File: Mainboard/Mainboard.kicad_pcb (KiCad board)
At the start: 4 copper layers, 78.8 x 40 mm, 55 parts, among them IC1 IP5306, J1 2479774-2, J3 Conn_01x06_Pin, U1 LM3880, U2 MAX98357A, U3 TPS22917DBV, U4 TLV62569DBV, U5 W25Q128JVS, U6 TLV75518PDBV, U7 TPS62822DLC

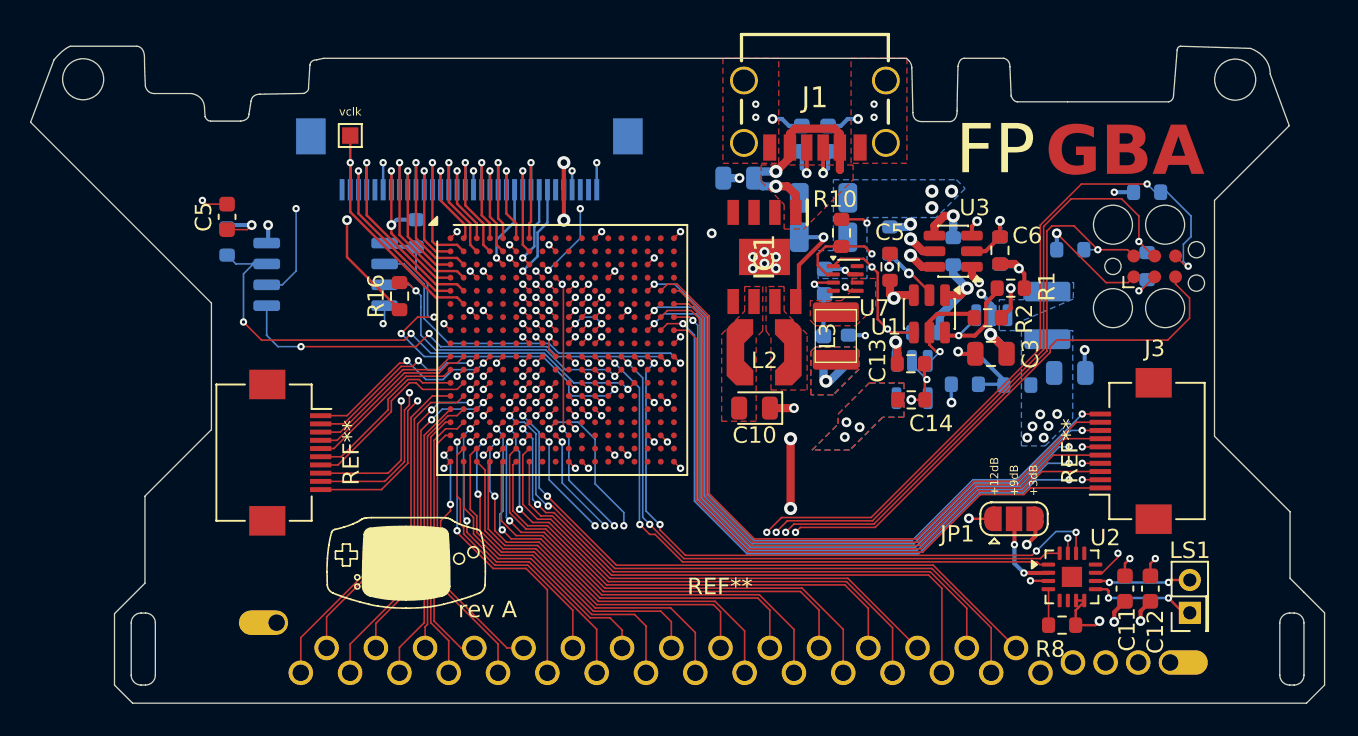
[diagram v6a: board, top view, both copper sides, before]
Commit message: + Power sw, + R arrays, sync PCB/schem
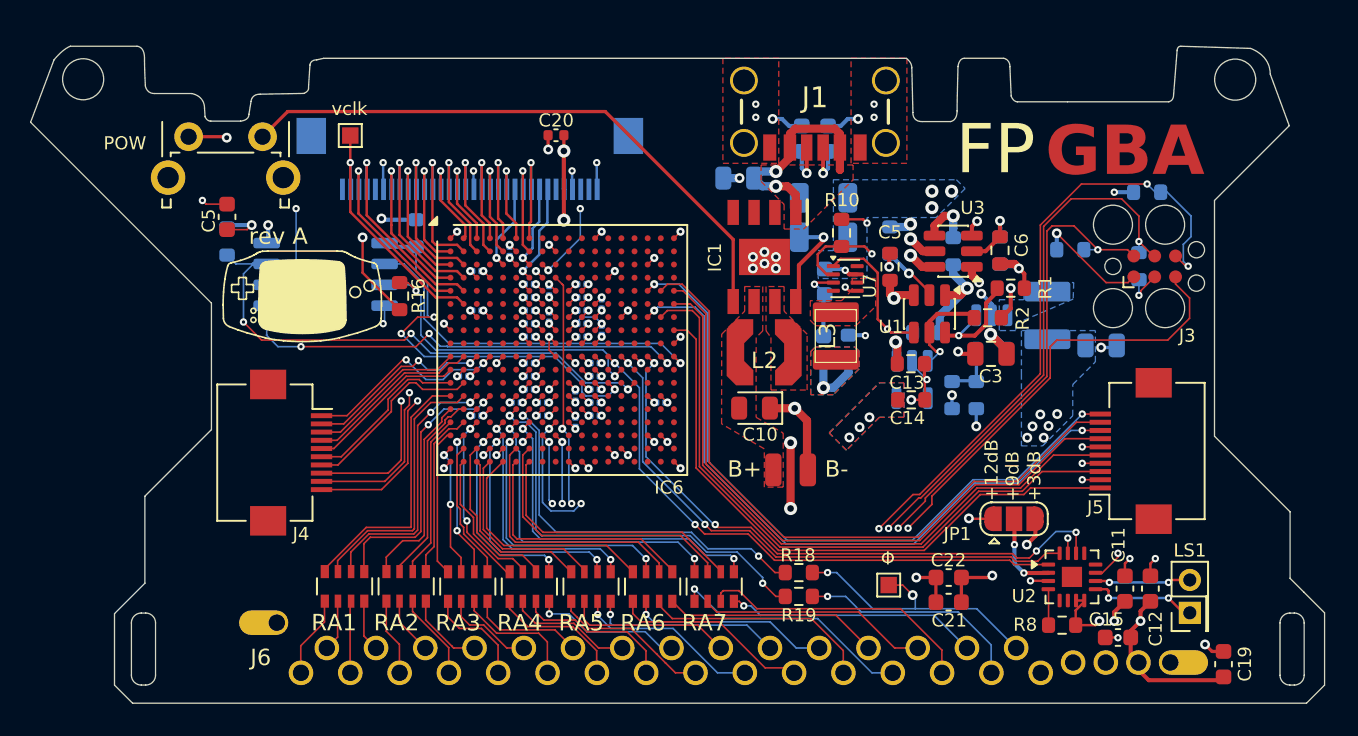
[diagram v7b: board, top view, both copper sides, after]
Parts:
- removed the REF** at (118.4, 77.1)
- removed the REF** at (153.0, 83.2)
- removed the REF** at (128.0, 92.0)
- removed the REF** at (101.8, 83.3)
- removed the REF** at (112.8, 65.5)
- added B+: SolderWirePad_1x01_SMD_1x2mm, Connector_Wire:SolderWirePad_1x01_SMD_1x2mm, F.Cu at (131.2, 84.4)
- added B-: SolderWirePad_1x01_SMD_1x2mm, Connector_Wire:SolderWirePad_1x01_SMD_1x2mm, F.Cu at (133.3, 84.4)
- added C15: 100nF, Capacitor_SMD:C_0603_1608Metric, F.Cu at (152.2, 94.6)
- added C19: 100nF, Capacitor_SMD:C_0603_1608Metric, F.Cu at (158.7, 96.2)
- added C20: 100nF, Capacitor_SMD:C_0402_1005Metric, F.Cu at (118.0, 64.0)
- added C21: 100nF, Capacitor_SMD:C_0603_1608Metric, F.Cu at (141.9, 92.5)
- added C22: 10uF, Capacitor_SMD:C_0603_1608Metric, F.Cu at (141.9, 91.0)
- added IC6: XC7S50-L1CSGA324I, Package_BGA:BGA-324_15x15mm_Layout18x18_P0.8mm, F.Cu at (118.4, 77.1)
- added J4: Left Daughter Connector, Connector_FFC-FPC:Hirose_FH12-10S-0.5SH_1x10-1MP_P0.50mm_Horizontal, F.Cu at (101.9, 83.3)
- added J5: Right Daughter Connector, Connector_FFC-FPC:Hirose_FH12-10S-0.5SH_1x10-1MP_P0.50mm_Horizontal, F.Cu at (153.0, 83.2)
- added J6: CART, AGBRE:AGB Cart Pin, F.Cu at (128.0, 92.0)
- added J9: Screen zif FFC/FPC, Connector_FFC-FPC:Hirose_FH12-32S-0.5SH_1x32-1MP_P0.50mm_Horizontal, B.Cu at (112.8, 65.5)
- added R18: 22, Resistor_SMD:R_0603_1608Metric, F.Cu at (132.8, 90.7)
- added R19: 22, Resistor_SMD:R_0603_1608Metric, F.Cu at (132.8, 92.1)
- added RA1: 22, Resistor_SMD:R_Array_Convex_4x0603, F.Cu at (105.2, 91.5)
- added RA2: 22, Resistor_SMD:R_Array_Convex_4x0603, F.Cu at (108.9, 91.5)
- added RA3: 22, Resistor_SMD:R_Array_Convex_4x0603, F.Cu at (112.7, 91.5)
- added RA4: 22, Resistor_SMD:R_Array_Convex_4x0603, F.Cu at (116.4, 91.5)
- added RA5: 22, Resistor_SMD:R_Array_Convex_4x0603, F.Cu at (120.2, 91.5)
- added RA6: 22, Resistor_SMD:R_Array_Convex_4x0603, F.Cu at (123.9, 91.5)
- added RA7: 22, Resistor_SMD:R_Array_Convex_4x0603, F.Cu at (127.7, 91.5)
- added REF**: C_0201_0603Metric, Capacitor_SMD:C_0201_0603Metric, B.Cu at (119.6, 73.9)
- added REF**: C_0201_0603Metric, Capacitor_SMD:C_0201_0603Metric, B.Cu at (112.4, 78.7)
- added REF**: C_0201_0603Metric, Capacitor_SMD:C_0201_0603Metric, B.Cu at (116.4, 76.3)
- added REF**: C_0201_0603Metric, Capacitor_SMD:C_0201_0603Metric, B.Cu at (113.2, 81.1)
- added REF**: C_0201_0603Metric, Capacitor_SMD:C_0201_0603Metric, B.Cu at (113.2, 74.7)
- added REF**: C_0201_0603Metric, Capacitor_SMD:C_0201_0603Metric, B.Cu at (115.2, 71.1)
- added REF**: C_0201_0603Metric, Capacitor_SMD:C_0201_0603Metric, B.Cu at (120.4, 80.3)
- added REF**: C_0201_0603Metric, Capacitor_SMD:C_0201_0603Metric, B.Cu at (119.6, 75.5)
- added REF**: C_0201_0603Metric, Capacitor_SMD:C_0201_0603Metric, B.Cu at (120.4, 77.9)
- added REF**: C_0201_0603Metric, Capacitor_SMD:C_0201_0603Metric, B.Cu at (120.4, 79.5)
- added REF**: C_0201_0603Metric, Capacitor_SMD:C_0201_0603Metric, B.Cu at (117.2, 80.3)
- added REF**: C_0201_0603Metric, Capacitor_SMD:C_0201_0603Metric, B.Cu at (115.6, 80.3)
- added REF**: C_0201_0603Metric, Capacitor_SMD:C_0201_0603Metric, B.Cu at (124.4, 80.3)
- added REF**: C_0201_0603Metric, Capacitor_SMD:C_0201_0603Metric, B.Cu at (116.4, 75.5)
- added REF**: C_0201_0603Metric, Capacitor_SMD:C_0201_0603Metric, B.Cu at (120.8, 74.3)
- added REF**: C_0201_0603Metric, Capacitor_SMD:C_0201_0603Metric, B.Cu at (120.8, 75.9)
- added REF**: C_0201_0603Metric, Capacitor_SMD:C_0201_0603Metric, B.Cu at (119.2, 81.5)
- added REF**: C_0201_0603Metric, Capacitor_SMD:C_0201_0603Metric, B.Cu at (116.4, 79.5)
- added REF**: C_0201_0603Metric, Capacitor_SMD:C_0201_0603Metric, B.Cu at (116.4, 73.1)
- added REF**: C_0201_0603Metric, Capacitor_SMD:C_0201_0603Metric, B.Cu at (117.2, 81.1)
- added REF**: C_0201_0603Metric, Capacitor_SMD:C_0201_0603Metric, B.Cu at (120.4, 78.7)
- added REF**: C_0201_0603Metric, Capacitor_SMD:C_0201_0603Metric, B.Cu at (116.4, 77.9)
- added REF**: C_0201_0603Metric, Capacitor_SMD:C_0201_0603Metric, B.Cu at (113.2, 72.3)
- added REF**: C_0201_0603Metric, Capacitor_SMD:C_0201_0603Metric, B.Cu at (120.4, 81.1)
- added REF**: C_0201_0603Metric, Capacitor_SMD:C_0201_0603Metric, B.Cu at (116.4, 73.9)
- added REF**: C_0201_0603Metric, Capacitor_SMD:C_0201_0603Metric, B.Cu at (119.6, 73.1)
- added REF**: C_0201_0603Metric, Capacitor_SMD:C_0201_0603Metric, B.Cu at (119.6, 76.3)
- added REF**: C_0201_0603Metric, Capacitor_SMD:C_0201_0603Metric, B.Cu at (117.6, 73.5)
- added REF**: C_0201_0603Metric, Capacitor_SMD:C_0201_0603Metric, B.Cu at (119.6, 74.7)
- added REF**: C_0201_0603Metric, Capacitor_SMD:C_0201_0603Metric, B.Cu at (117.6, 75.1)
- added REF**: C_0201_0603Metric, Capacitor_SMD:C_0201_0603Metric, B.Cu at (116.4, 74.7)
- added REF**: C_0201_0603Metric, Capacitor_SMD:C_0201_0603Metric, B.Cu at (116.4, 78.7)
- added REF**: C_0201_0603Metric, Capacitor_SMD:C_0201_0603Metric, B.Cu at (119.2, 79.9)
- added SW1: POW, Button_Switch_THT:SW_Tactile_SPST_Angled_PTS645Vx58-2LFS, F.Cu at (95.7, 64.1)
- added Φ: test, TestPoint:TestPoint_Pad_1.0x1.0mm, F.Cu at (138.3, 91.4)
- R4: value 100k -> 180k
- moved R4 2.57 mm to (143.6, 79.8), turned to 90 degrees
- moved C4 2.54 mm to (151.2, 76.8)
- moved R7 1.02 mm to (142.1, 79.8), turned to -90 degrees
- moved R14 0.50 mm to (153.5, 72.0)
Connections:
- net /FPGBA Charging/BAT renamed Net-(BT1-+)
- net /FPGBA_Power/REF1V renamed REF1V
- net /FPGBA_Power/VREF1V8 renamed VREF1V8
- net /FPGBA_Power/VREF5V renamed VREF5V
- vclk pad 1: (no net) -> /FPGA/DCLK
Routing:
- net (no net): track 1377.3 -> 0.00 mm, vias 65 -> 0
- net Net-(IC6-IO_L10P_T1_AD11P_15): track 0.00 -> 42.6 mm, vias 0 -> 2
- net Net-(IC6-IO_L14P_T2_SRCC_15): track 0.00 -> 41.8 mm, vias 0 -> 2
- net Net-(IC6-IO_L10N_T1_AD11N_15): track 0.00 -> 41.6 mm
- net /FPGA/PHI: track 0.00 -> 40.4 mm, vias 0 -> 4
- net Net-(IC6-IO_L16N_T2_15): track 0.00 -> 40.2 mm
- net Net-(IC6-IO_L14N_T2_SRCC_15): track 0.00 -> 40.1 mm
- net Net-(IC6-IO_L16P_T2_15): track 0.00 -> 39.5 mm
- net /FPGA/WR: track 0.00 -> 39.4 mm, vias 0 -> 3
- net Net-(IC6-IO_L21P_T3_DQS_15): track 0.00 -> 37.7 mm
- net unconnected-(IC1-KEY-Pad5): track 0.00 -> 36.3 mm
- net /FPGA/RD: track 0.00 -> 36.1 mm, vias 0 -> 3
- net /FPGA/AD1: track 0.00 -> 34.4 mm, vias 0 -> 3
- net /FPGA/CS: track 0.00 -> 33.6 mm
- net /FPGA/AD0: track 0.00 -> 31.3 mm
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
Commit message: updated damping resistors
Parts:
- removed R18, R19: 22, Resistor_SMD:R_0603_1608Metric
- removed RA1, RA2, RA3, RA4, RA5, RA6, RA7: 22, Resistor_SMD:R_Array_Convex_4x0603
- added DR: 22, Resistor_SMD:R_0402_1005Metric, F.Cu at (148.9, 85.5)
- added DR: 22, Resistor_SMD:R_0402_1005Metric, F.Cu at (142.6, 89.6)
- added DR: 22, Resistor_SMD:R_0402_1005Metric, F.Cu at (145.5, 84.5)
- added DR: 22, Resistor_SMD:R_0402_1005Metric, F.Cu at (128.7, 91.5)
- added DR: 22, Resistor_SMD:R_0402_1005Metric, F.Cu at (126.5, 92.0)
- added DR: 22, Resistor_SMD:R_0402_1005Metric, F.Cu at (141.3, 85.1)
- added DR: 22, Resistor_SMD:R_0402_1005Metric, F.Cu at (122.5, 90.8)
- added DR: 22, Resistor_SMD:R_0402_1005Metric, F.Cu at (121.5, 89.0)
- added DR: 22, Resistor_SMD:R_0402_1005Metric, F.Cu at (126.5, 90.9)
- added DR: 22, Resistor_SMD:R_0402_1005Metric, F.Cu at (126.4, 94.7)
- added DR: 22, Resistor_SMD:R_0402_1005Metric, F.Cu at (121.8, 91.6)
- added DR: 22, Resistor_SMD:R_0402_1005Metric, F.Cu at (128.7, 90.4)
- added DR: 22, Resistor_SMD:R_0402_1005Metric, F.Cu at (148.9, 83.5)
- added DR: 22, Resistor_SMD:R_0402_1005Metric, F.Cu at (132.4, 94.5)
- added DR: 22, Resistor_SMD:R_0402_1005Metric, F.Cu at (144.6, 90.2)
- added DR: 22, Resistor_SMD:R_0402_1005Metric, F.Cu at (120.7, 89.8)
- added DR: 22, Resistor_SMD:R_0402_1005Metric, F.Cu at (142.6, 88.6)
- added DR: 22, Resistor_SMD:R_0402_1005Metric, F.Cu at (143.1, 84.1)
- added DR: 22, Resistor_SMD:R_0402_1005Metric, F.Cu at (135.1, 86.8)
- added DR: 22, Resistor_SMD:R_0402_1005Metric, F.Cu at (146.1, 83.5)
- added DR: 22, Resistor_SMD:R_0402_1005Metric, F.Cu at (142.3, 83.3)
- added DR: 22, Resistor_SMD:R_0402_1005Metric, F.Cu at (129.4, 94.5)
- added DR: 22, Resistor_SMD:R_0402_1005Metric, F.Cu at (135.1, 87.8)
- added DR: 22, Resistor_SMD:R_0402_1005Metric, F.Cu at (125.7, 66.1)
- added DR: 22, Resistor_SMD:R_0402_1005Metric, F.Cu at (148.9, 84.5)
- added DR: 22, Resistor_SMD:R_0402_1005Metric, F.Cu at (140.5, 84.4)
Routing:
- net Net-(IC6-IO_L10P_T1_AD11P_15): track 42.6 -> 48.2 mm, vias 2 -> 4
- net Net-(IC6-IO_L14P_T2_SRCC_15): track 41.8 -> 46.6 mm, vias 2 -> 4
- net /FPGA/AD3: track 29.8 -> 26.4 mm
- net /FPGA/AD1: track 34.4 -> 31.1 mm
- net Net-(IC6-IO_L21P_T3_DQS_15): track 37.7 -> 34.9 mm
- net /FPGA/AD5: track 26.5 -> 23.8 mm
- net /FPGA/AD8: track 21.7 -> 19.3 mm
- net /FPGA/AD4: track 28.5 -> 26.2 mm, vias 3 -> 2
- net /FPGA/AD2: track 28.3 -> 26.1 mm
- net /FPGA/AD10: track 21.2 -> 19.0 mm, vias 3 -> 1
- net /FPGA/CS: track 33.6 -> 31.6 mm
- net /FPGA/AD7: track 25.7 -> 23.8 mm, vias 3 -> 2
- net /FPGA/AD0: track 31.3 -> 29.7 mm
- net /FPGA/IRQ/DREQ: track 21.1 -> 22.7 mm
- net /FPGA/AD11: track 19.8 -> 18.2 mm
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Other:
- board text added: "22"
